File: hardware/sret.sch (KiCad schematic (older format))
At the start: 101 parts, among them CON1 SD_Card, J1 RJ45-TRANSFO, P1 USB0, P10 CONN_02X04, P11 USB1, P12 CONN_02X01, P13 CONN_02X01, P2 CONN_02X01, P3 CONN_02X01, P4 CONN_02X01, P5 CONN_02X01, P6 CONN_01X06, P7 CONN_01X06, P8 CONN_01X06, P9 CONN_01X06, SW1 DFU, SW2 RESET, U1 LPC4330, U2 DRTR5V0U2SR, U3 W25Q80BV, U4 LAN8742A, U5 MAX3051, U6 MAX3051, U7 TC1262, X1 CRYSTAL_SMD, X2 CRYSTAL_SMD, Y1 RTC

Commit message: rough pcb layout
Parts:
- removed FB3: FILTER, Resistors_SMD:R_0805_HandSoldering, symbol FILTER
- added W1, W2, W3, W4: Mount, Mounting_Holes:MountingHole_2-5mm, symbol TEST_1P
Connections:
- net U0_RXD is gone; now on net U0_RX: U1.82 (U0_RXD)
- net U0_TXD is gone; now on net U0_TX: U1.80 (U0_TXD)
- net GND: now also W1.1, W2.1, W3.1, W4.1
- net VCC: now also R31.1, R32.1, R33.1, R34.1
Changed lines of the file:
@@
 U1_RXD/EMC_D11
 Text Label 7500 4850 0    60   ~ 0
-U0_TXD
+U0_TX
 Text Label 7500 4750 0    60   ~ 0
 SGPIO2/EMC_A12
@@
 SGPIO2/EMC_A12
 Text Label 7500 4650 0    60   ~ 0
-U0_RXD
+U0_RX
 Text Label 7500 4550 0    60   ~ 0
 EMC_BLS1#
@@
 L VCC #PWR078
 U 1 1 58CFFDE4
-P 7350 7100
-F 0 "#PWR078" H 7350 6950 50  0001 C CNN
-F 1 "VCC" H 7350 7250 50  0000 C CNN
-F 2 "" H 7350 7100 50  0000 C CNN
-F 3 "" H 7350 7100 50  0000 C CNN
-	1    7350 7100
+P 7350 7750
+F 0 "#PWR078" H 7350 7600 50  0001 C CNN
+F 1 "VCC" H 7350 7900 50  0000 C CNN
+F 2 "" H 7350 7750 50  0000 C CNN
+F 3 "" H 7350 7750 50  0000 C CNN
+	1    7350 7750
 	1    0    0    -1
 $EndComp
@@
 	1    2050 7100
 	1    0    0    -1
-$EndComp
-$Comp
-L FILTER FB3
-U 1 1 58CF2A65
-P 7350 7450
-F 0 "FB3" H 7350 7600 50  0000 C CNN
-F 1 "FILTER" H 7350 7350 50  0000 C CNN
-F 2 "Resistors_SMD:R_0805_HandSoldering" H 7350 7450 50  0001 C CNN
-F 3 "" H 7350 7450 50  0000 C CNN
-	1    7350 7450
-	0    1    1    0
 $EndComp
 Text Label 15300 6300 0    60   ~ 0
@@
 Connection ~ 7800 9500
 Wire Wire Line
-	7350 7800 7350 7950
+	7350 7750 7350 7950
 Wire Wire Line
 	7350 7900 7800 7900
@@
 Connection ~ 2700 650
 Connection ~ 2900 650
+Wire Wire Line
+	2950 8450 2950 8550
+Wire Wire Line
+	2700 8450 2700 8550
+$Comp
+L GND #PWR089
+U 1 1 58DAD82E
+P 2700 8550
+F 0 "#PWR089" H 2700 8300 50  0001 C CNN
+F 1 "GND" H 2700 8400 50  0000 C CNN
+F 2 "" H 2700 8550 50  0000 C CNN
+F 3 "" H 2700 8550 50  0000 C CNN
+	1    2700 8550
+	1    0    0    -1
+$EndComp
+$Comp
+L GND #PWR090
+U 1 1 58DADEC0
+P 2950 8550
+F 0 "#PWR090" H 2950 8300 50  0001 C CNN
+F 1 "GND" H 2950 8400 50  0000 C CNN
+F 2 "" H 2950 8550 50  0000 C CNN
+F 3 "" H 2950 8550 50  0000 C CNN
+	1    2950 8550
+	1    0    0    -1
+$EndComp
+$Comp
+L GND #PWR091
+U 1 1 58DADF67
+P 3200 8550
+F 0 "#PWR091" H 3200 8300 50  0001 C CNN
+F 1 "GND" H 3200 8400 50  0000 C CNN
+F 2 "" H 3200 8550 50  0000 C CNN
+F 3 "" H 3200 8550 50  0000 C CNN
+	1    3200 8550
+	1    0    0    -1
+$EndComp
+$Comp
+L GND #PWR092
+U 1 1 58DADF74
+P 3450 8550
+F 0 "#PWR092" H 3450 8300 50  0001 C CNN
+F 1 "GND" H 3450 8400 50  0000 C CNN
+F 2 "" H 3450 8550 50  0000 C CNN
+F 3 "" H 3450 8550 50  0000 C CNN
+	1    3450 8550
+	1    0    0    -1
+$EndComp
+Wire Wire Line
+	3450 8450 3450 8550
+Wire Wire Line
+	3200 8450 3200 8550
+$Comp
+L TEST_1P W3
+U 1 1 58DADF61
+P 3200 8450
+F 0 "W3" H 3200 8720 50  0000 C CNN
+F 1 "Mount" H 3200 8650 50  0000 C CNN
+F 2 "Mounting_Holes:MountingHole_2-5mm" H 3400 8450 50  0001 C CNN
+F 3 "" H 3400 8450 50  0000 C CNN
+	1    3200 8450
+	1    0    0    -1
+$EndComp
+$Comp
+L TEST_1P W1
+U 1 1 58DAD71B
+P 2700 8450
+F 0 "W1" H 2700 8720 50  0000 C CNN
+F 1 "Mount" H 2700 8650 50  0000 C CNN
+F 2 "Mounting_Holes:MountingHole_2-5mm" H 2900 8450 50  0001 C CNN
+F 3 "" H 2900 8450 50  0000 C CNN
+	1    2700 8450
+	1    0    0    -1
+$EndComp
+$Comp
+L TEST_1P W2
+U 1 1 58DADEBA
+P 2950 8450
+F 0 "W2" H 2950 8720 50  0000 C CNN
+F 1 "Mount" H 2950 8650 50  0000 C CNN
+F 2 "Mounting_Holes:MountingHole_2-5mm" H 3150 8450 50  0001 C CNN
+F 3 "" H 3150 8450 50  0000 C CNN
+	1    2950 8450
+	1    0    0    -1
+$EndComp
+$Comp
+L TEST_1P W4
+U 1 1 58DADF6E
+P 3450 8450
+F 0 "W4" H 3450 8720 50  0000 C CNN
+F 1 "Mount" H 3450 8650 50  0000 C CNN
+F 2 "Mounting_Holes:MountingHole_2-5mm" H 3650 8450 50  0001 C CNN
+F 3 "" H 3650 8450 50  0000 C CNN
+	1    3450 8450
+	1    0    0    -1
+$EndComp
 $EndSCHEMATC

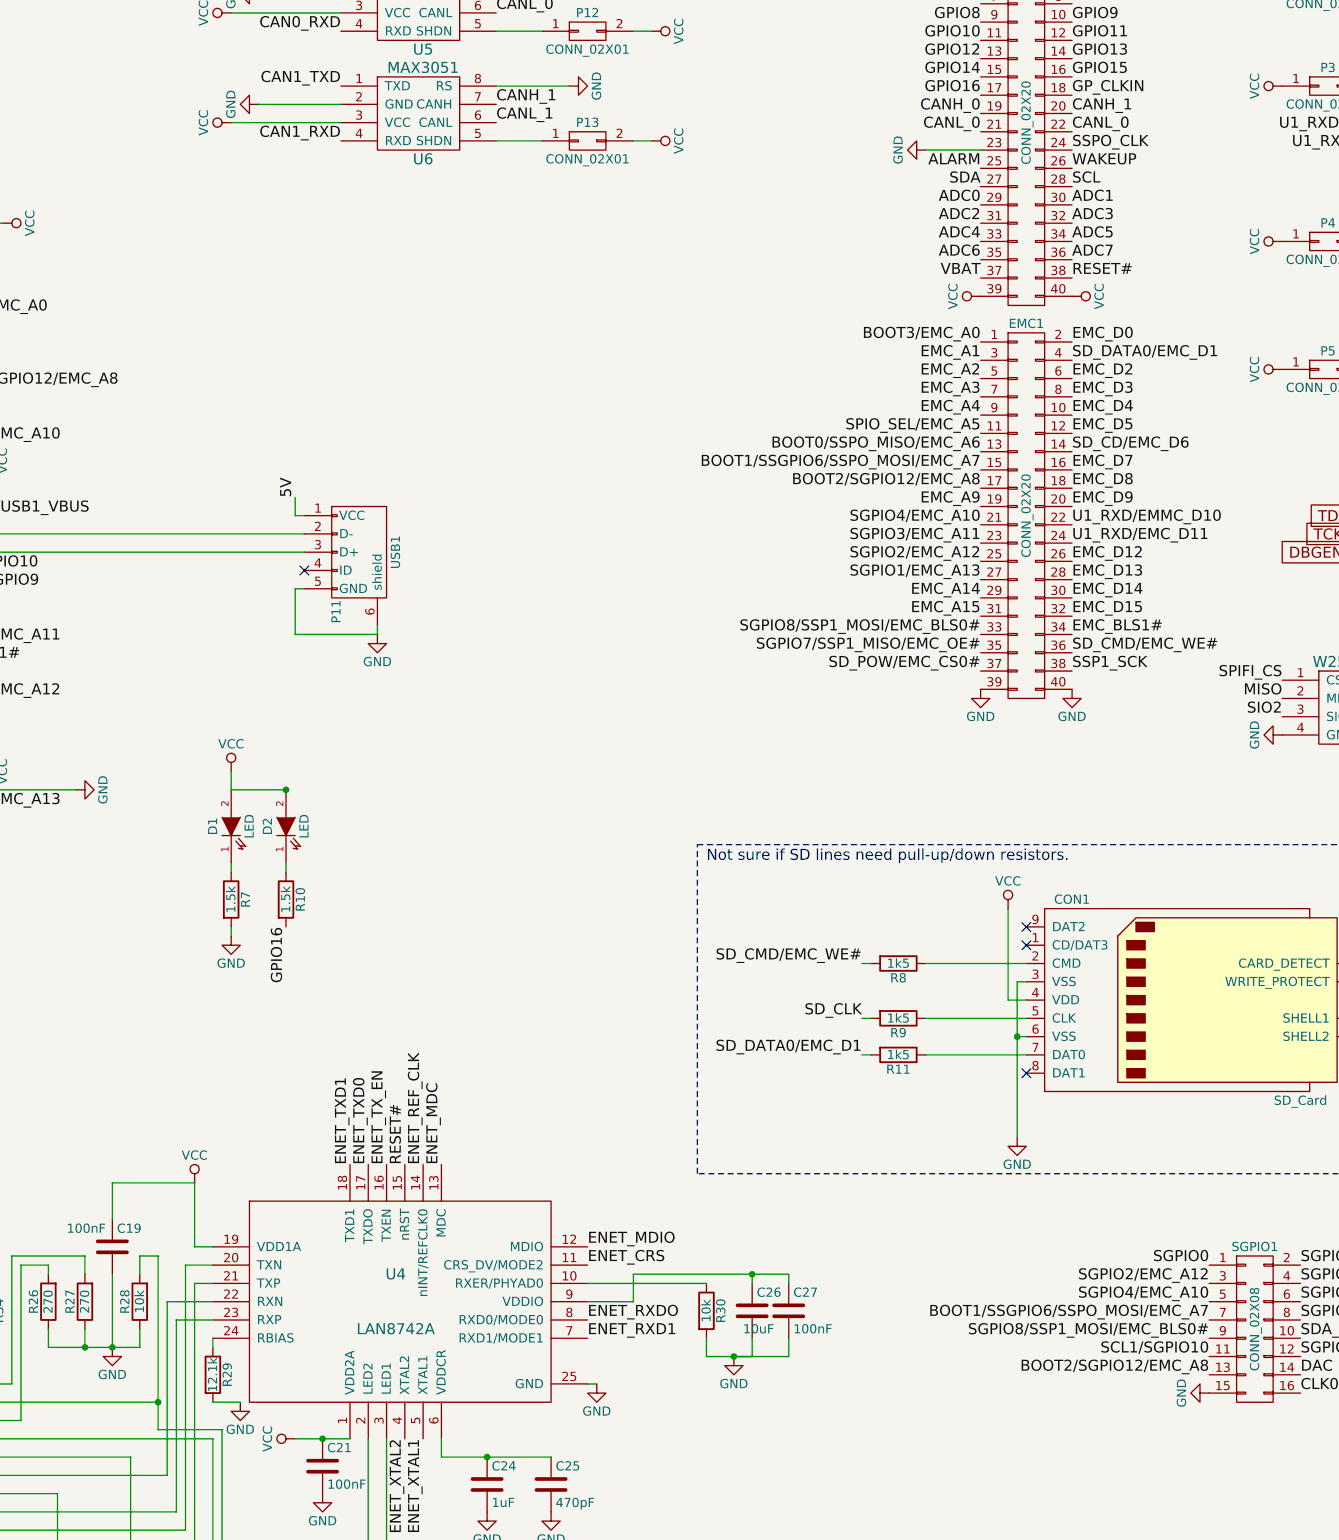
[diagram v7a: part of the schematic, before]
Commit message: added RS485/IEBus chip
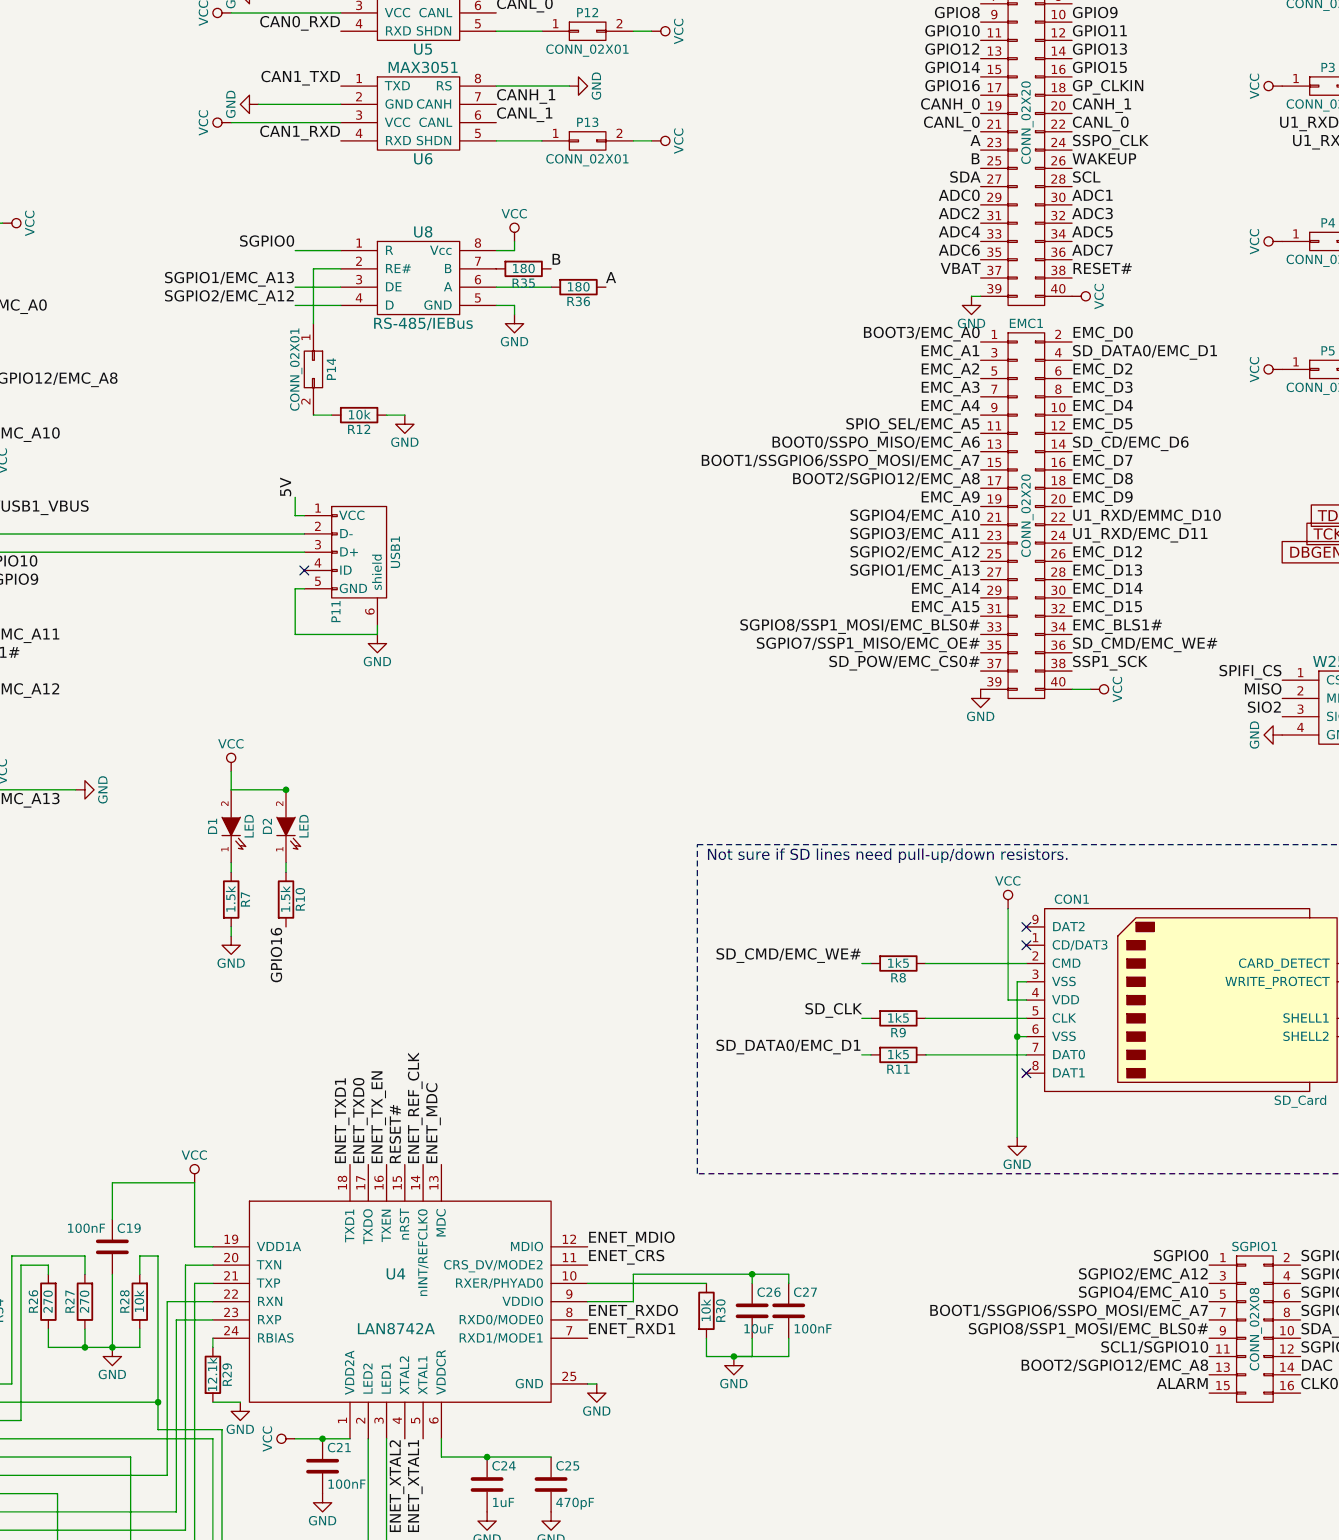
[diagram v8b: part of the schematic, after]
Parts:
- added P14: CONN_02X01, Pin_Headers:Pin_Header_Straight_2x01, symbol CONN_02X01
- added R12: 10k, Resistors_SMD:R_0603_HandSoldering, symbol R
- added R35, R36: 180, Resistors_SMD:R_0603_HandSoldering, symbol R
- added U8: RS-485/IEBus, SMD_Packages:SOIC-8-N, symbol RS-485/IEBus
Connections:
- net ALARM: now also SGPIO1.15 (P15); no longer GPIO1.25 (P25)
- net GND: now also GPIO1.39 (P39), R12.1, U8.5 (GND); no longer EMC1.40 (P40), GPIO1.23 (P23), SGPIO1.15 (P15)
- net SGPIO0: now also U8.1 (R)
- net SGPIO1/EMC_A13: now also U8.3 (DE)
- net SGPIO2/EMC_A12: now also U8.4 (D)
- net VCC: now also EMC1.40 (P40), U8.8 (Vcc); no longer GPIO1.39 (P39)
- new net: P14.1 (P1), U8.2 (RE#)
- new net: R36.2, U8.6 (A)
- new net: R35.2, U8.7 (B)
- new net: P14.2 (P2), R12.2
- new net A: GPIO1.23 (P23), R36.1
- new net B: GPIO1.25 (P25), R35.1
